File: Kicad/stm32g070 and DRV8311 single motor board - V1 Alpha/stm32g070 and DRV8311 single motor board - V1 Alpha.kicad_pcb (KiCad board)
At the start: 4 copper layers, 38.8 x 42.1 mm, 75 parts, among them J1 JST SH SM04B, J2 JST SH SM06B, J3 Molex_PicoBlade_53048-0310 Ho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, J4 Conn_01x02_Pin, Q1 NMOS, SQS142ENW, Q2 NMOS, Q3 PMOS,SiSS61DN, Q4 PMOS, SW1 SW_Push, U1 STM32G070CBTr, U2 DRV8311HRRWR, U3 BQ298012RUGT, U4 BQ25060, Y1 ABM8-16.000MHZ-10-1-U-T

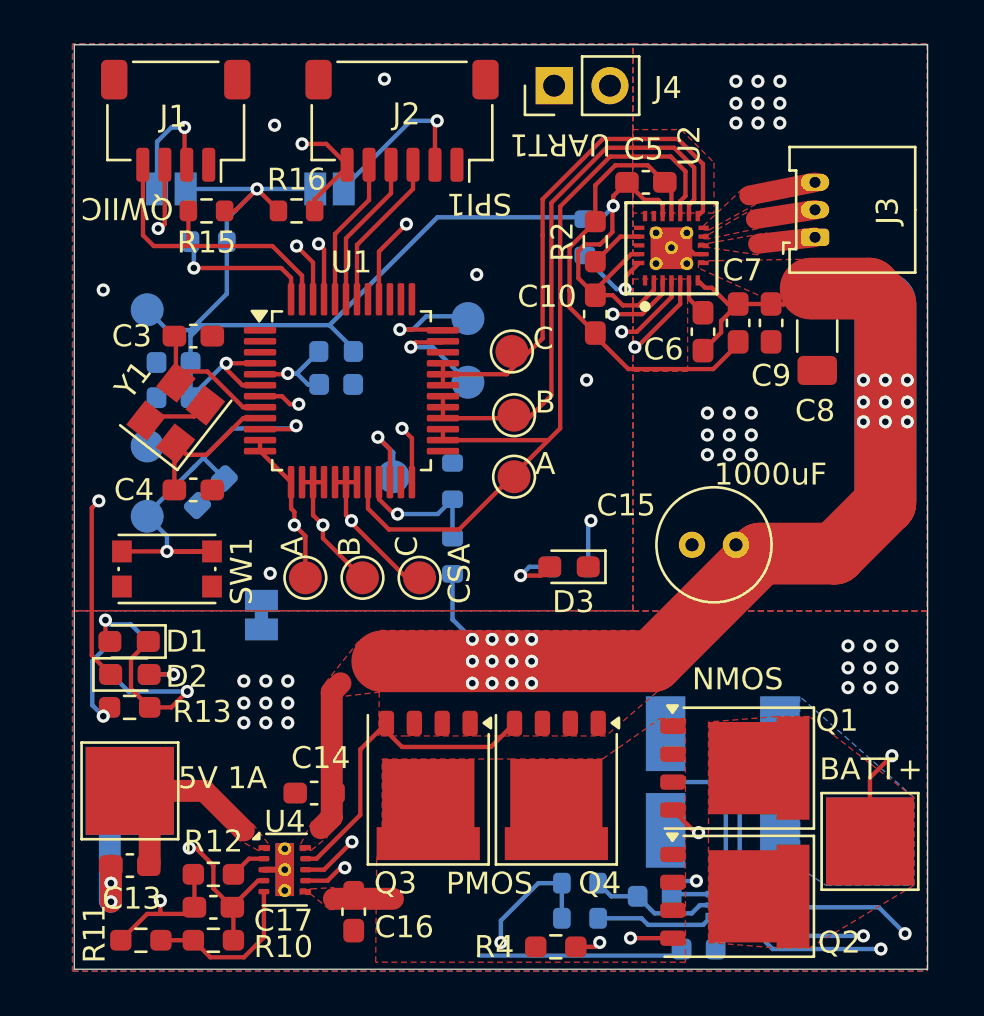
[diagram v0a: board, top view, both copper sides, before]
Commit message: Fixes to the PCB after production related to mosfets
So..... I sourced the wrong mosfets. I chose mosfets with the marketing moniker PowerPAK, never thinking that could mean multiple footprint sizes. I sourced mosfets with the powerpak 1212 footprint, instead of the powerpak SO-8 footprint. They ended up being tiny and I had to do a bodge fix to test. I have replaced the mosfets in schematic with correctly sized ones now.

Another change I made in this commit is related to LEDs. I sourced the leds and resistors last minute, so the values are a bit different than originally on the schematic. I realized too that my tri-state led status circuit wouldn't work, because the bq25060 status pin is not a tri-state and I couldn't make it one. I now only have one led to indicate charging. I have updated the schematics and board with the values and single status led.

The big capacitors I sourced differently, I wasn't able to get a small 220uF, so I got a big aluminum polarized 220uF and put it in place of the 1000uF. All the other capacitors are different too, I realized the voltage rating doesn't matter on some, so to cut down BOM part number if there was a capacitor value with two separate voltages, I just went with 16v one.

Gerber files have been updated.
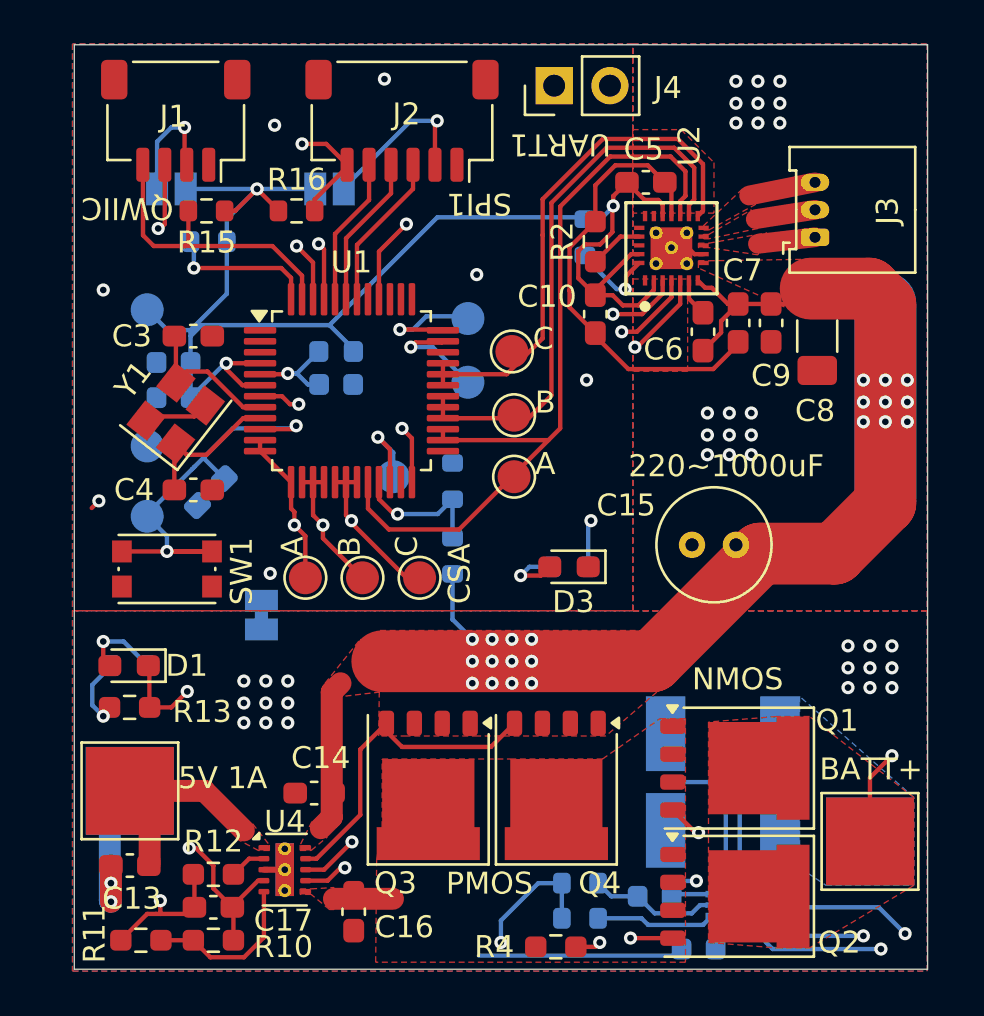
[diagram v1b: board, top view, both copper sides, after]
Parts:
- removed D2: green_LED, LED_SMD:LED_0603_1608Metric_Pad1.05x0.95mm_HandSolder
- removed R9: 470 ohm, Resistor_SMD:R_0603_1608Metric
- C9: value 0.1uF, 16 v -> 0.1uF, 16v
- D1: value red_LED -> Osram LT Q99G.01 green led
- D3: value green_LED -> Osram LT Q99G.01 green led
- Q1: value NMOS, SQS142ENW -> NMOS, sir404dp
- Q3: value PMOS,SiSS61DN -> PMOS,Si7157DP
- R17: value 100k, or maybe 27k to get more range -> 100k
- R18: value 100k -> 150k
- R19: value 2k -> 80.6 ohm
- R8: value 2k -> 402 ohm
- moved R8 1.10 mm to (125.2, 116.4)
- moved D1 1.10 mm to (125.2, 116.4)
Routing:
- net GND: track 71.7 -> 63.7 mm
- net /PSU/~{CHG}: track 23.5 -> 17.9 mm
- net Net-(D2-A): track 2.29 -> 0.00 mm, vias 1 -> 0
- net /PSU/LDO 4.9v: track 29.4 -> 28.3 mm
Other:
- board text added: "220~1000uF"
- board text removed: "1000uF"

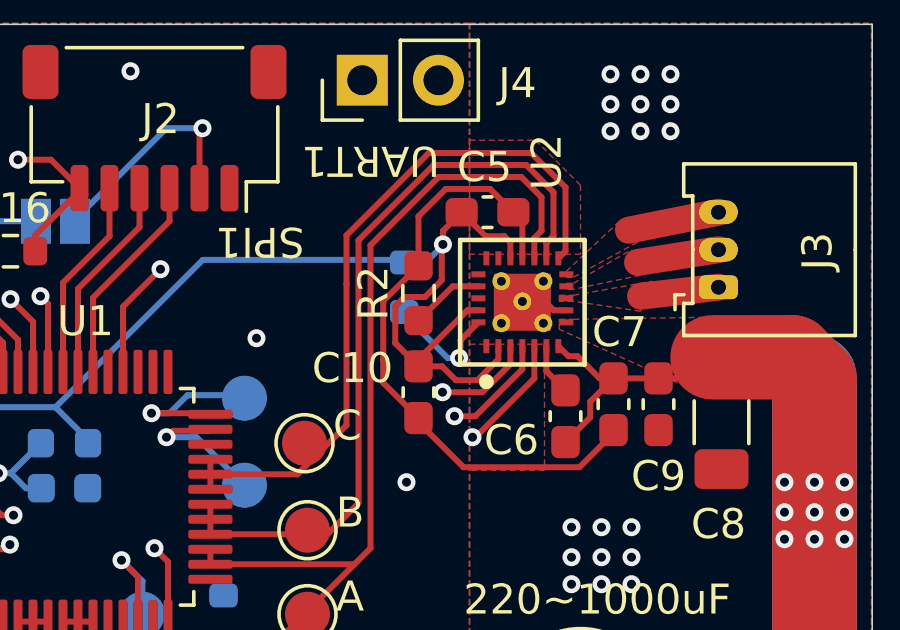
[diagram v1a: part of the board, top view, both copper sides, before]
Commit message: Fixing DRV8311 recursive design flaw, and pin tie issue
Since I'm using 3x pwm mode for the driver, I should have tied the unused lowside pins to 3.3v, and not left them floating, according to the datasheet. This is fixed now

The driver chip has an enable pin with an internal weak pulldown. I put a pull-up resistor on the outside, to always keep the chip on. Guess what that is connected to though? The regulator output from the chip, which is disabled! I fixed this in the design by have a voltage divider coming from motor power to enable the pin.
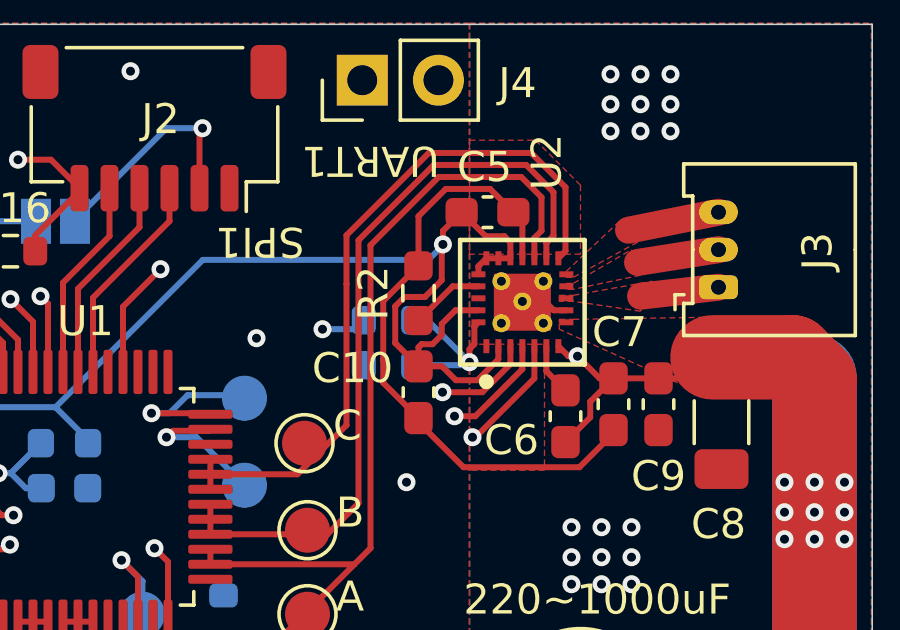
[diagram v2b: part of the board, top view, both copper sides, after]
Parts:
- added R9: 150k, Resistor_SMD:R_0603_1608Metric, B.Cu at (145.4, 99.5)
- R1: value 47k -> 100k
- moved R1 1.22 mm to (145.4, 98.0), turned to 180 degrees
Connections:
- R1 pad 1: VDD -> Net-(U2-SLEEP_N)
- R1 pad 2: Net-(U2-SLEEP_N) -> /MOTORPWR
- U2 pad 18: unconnected-(U2-INLA-Pad18) -> VDD
- U2 pad 19: unconnected-(U2-INLB-Pad19) -> VDD
- U2 pad 20: unconnected-(U2-INLC-Pad20) -> VDD
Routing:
- net /MOTORPWR: track 111.0 -> 121.4 mm, vias 21 -> 23
- net Net-(U2-SLEEP_N): track 3.88 -> 5.82 mm
- net VDD: track 67.9 -> 69.7 mm
